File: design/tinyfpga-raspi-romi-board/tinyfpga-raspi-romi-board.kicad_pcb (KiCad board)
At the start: 2 copper layers, 103.4 x 121.9 mm, 75 parts, among them J1 TINYFPGA_J1, J10 ROMI_ENC_LEFT, J11 ROMI_ENC_RIGHT, J12 QTR_LEFT, J13 QTR_RIGHT, J14 SONAR_LEFT, J15 SONAR_RIGHT, J16 PWR_SEL1, J17 PWR_SEL0, J19 ON_OFF, J2 TINYFPGA_J2, J20 ROMI_POWER, J3 Raspberry_Pi_2_3, J4 TINYFPGA_J4, J5 TINYFPGA_J5, J6 WP_JUMP, J7 ROMI_VSW, J8 FUSE_JUMP, J9 ROMI_MOTOR_DRIVE, Q1 2N7000, Q2 2N7000, Q3 2N7000, Q4 2N7000, Q5 2N7000, Q6 2N7000, Q7 2N7000, Q8 2N7000, SW2 SW_Push, SW3 SW_Push, SW4 SW_Push, U1 CAT24C128

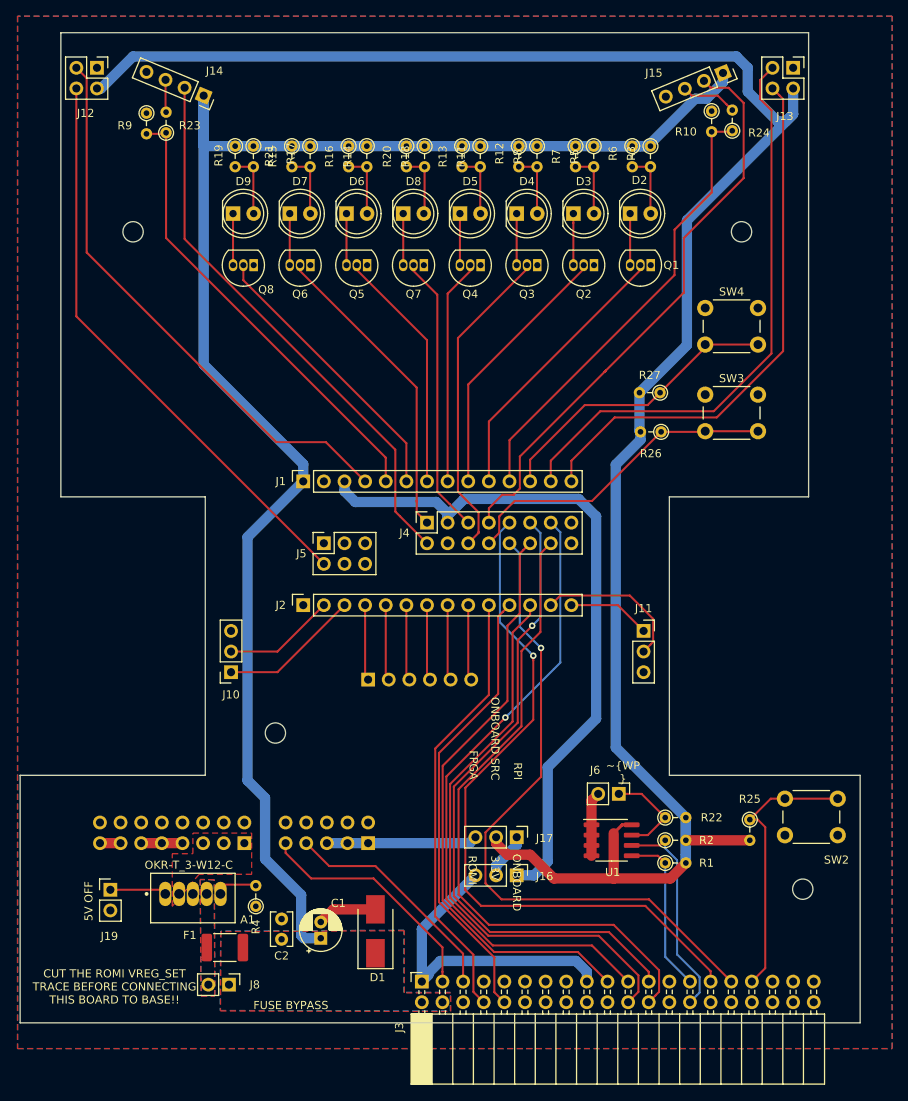
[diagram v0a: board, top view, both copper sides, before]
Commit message: changed mount hole size and aligned them better. added pwm pulldowns
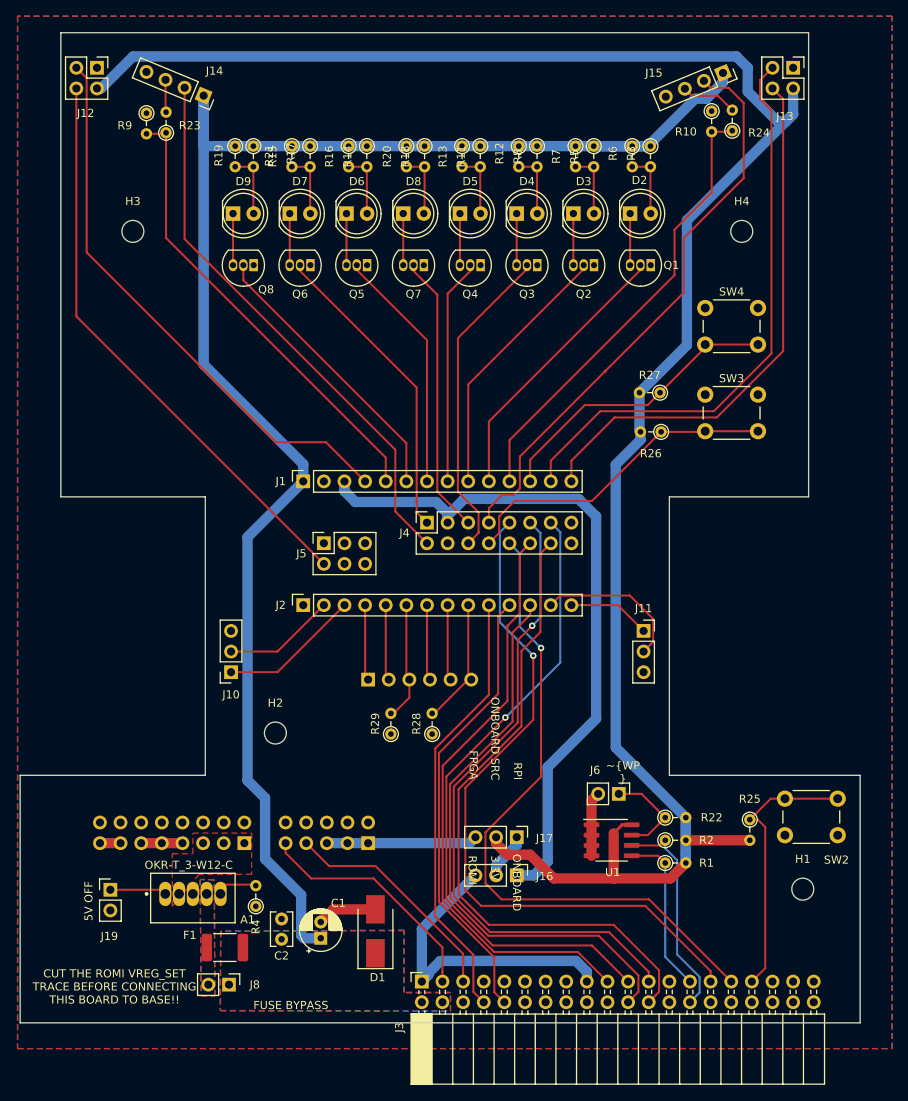
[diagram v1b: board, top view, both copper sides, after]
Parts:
- added R28: 3.9k, Resistor_THT:R_Axial_DIN0204_L3.6mm_D1.6mm_P2.54mm_Vertical, F.Cu at (103.5, 114.3)
- added R29: 3.9k, Resistor_THT:R_Axial_DIN0204_L3.6mm_D1.6mm_P2.54mm_Vertical, F.Cu at (98.4, 114.3)
- H1, H2, H3, H4: footprint MountingHole:MountingHole_2.5mm -> MountingHole:MountingHole_2.7mm_M2.5
- moved H4 0.06 mm to (141.6, 52.4)
- moved H3 0.06 mm to (66.6, 52.4)
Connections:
- J3 pad 11: (no net) -> /RPI_GPIO17
- J3 pad 12: (no net) -> /RPI_GPIO18
- J3 pad 13: (no net) -> Net-(J3-Pad13)
- J3 pad 15: (no net) -> /RPI_GPIO22
- J3 pad 16: (no net) -> /RPI_GPIO23
- J3 pad 18: (no net) -> /RPI_GPIO24
- J3 pad 26: (no net) -> /RPI_GPIO7
- J3 pad 32: (no net) -> /RPI_GPIO12
- J3 pad 35: (no net) -> /RPI_GPIO19
- J3 pad 36: (no net) -> /RPI_GPIO16
- J3 pad 37: (no net) -> Net-(J3-Pad37)
- J3 pad 38: (no net) -> /RPI_GPIO20
- J3 pad 40: (no net) -> /RPI_GPIO21
- J3 pad 7: (no net) -> Net-(J3-Pad7)
- J5 pad 1: (no net) -> /FPGA_CLK
- J5 pad 3: (no net) -> /FPGA_LED
- J5 pad 4: (no net) -> /FPGA_USB_PU
- J5 pad 5: (no net) -> /FPGA_USB_P
- J5 pad 6: (no net) -> /FPGA_USB_N
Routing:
- net /ROMI_PWMR: track 9.32 -> 15.9 mm
- net /ROMI_PWML: track 9.32 -> 14.6 mm
